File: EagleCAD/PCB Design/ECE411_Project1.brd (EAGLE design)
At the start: 160 x 100 mm, 24 parts

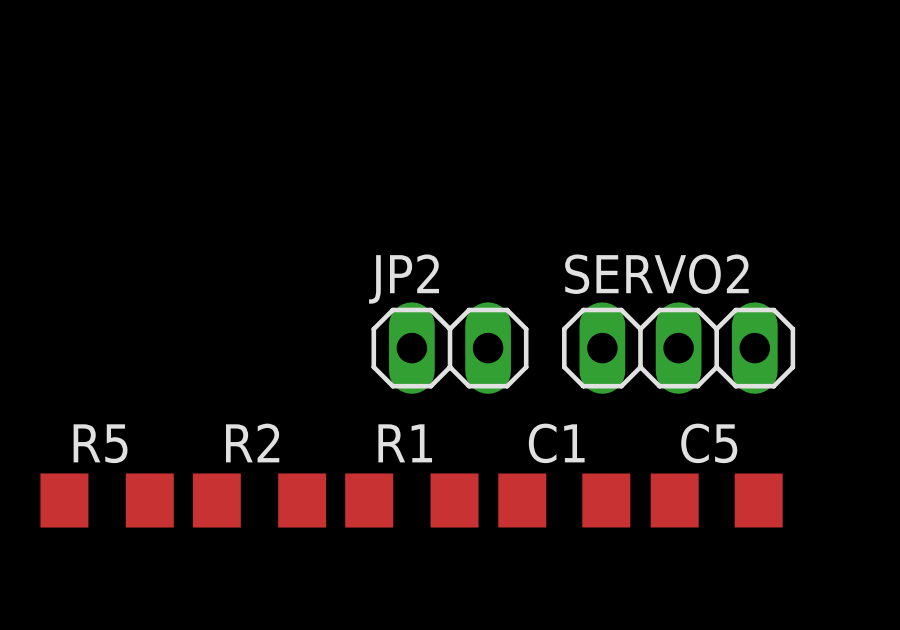
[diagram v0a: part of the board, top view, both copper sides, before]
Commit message: Added some custom library components, updated schematic with new xtal cap values, and updated links document
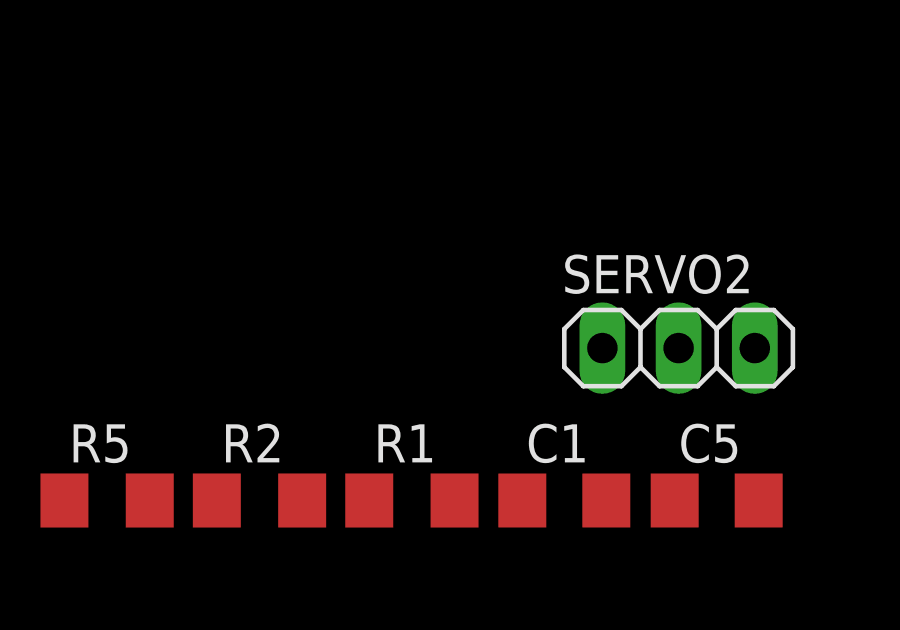
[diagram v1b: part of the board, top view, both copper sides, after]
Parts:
- removed JP2: (no value), pinhead:1X02
- C6, C7: value 12p -> 22p
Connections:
- net PWM1: now also SERVO1.1; no longer JP2.1
- net PWM2: now also SERVO2.1; no longer JP2.2
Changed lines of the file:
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@@
 <element name="CN1" library="adafruit" library_urn="urn:adsk.eagle:library:420" package="DCJACK_2MM_SMT" package3d_urn="urn:adsk.eagle:package:6240730/1" value="" x="-36.83" y="53.34"/>
 <element name="JP1" library="pinhead" library_urn="urn:adsk.eagle:library:325" package="2X03" package3d_urn="urn:adsk.eagle:package:22462/2" value="" x="-46.99" y="48.26"/>
-<element name="JP2" library="pinhead" library_urn="urn:adsk.eagle:library:325" package="1X02" package3d_urn="urn:adsk.eagle:package:22435/2" value="" x="-25.4" y="73.66"/>
 <element name="MICRO_USB_TYPE_B" library="adafruit" package="MOLEX_480371000" value="USB-A" x="-27.94" y="41.91">
 <attribute name="SPICEPREFIX" value="X" x="-27.94" y="41.91" size="1.778" layer="27" display="off"/>
@@
 <element name="LED2" library="led" library_urn="urn:adsk.eagle:library:259" package="1206" package3d_urn="urn:adsk.eagle:package:15796/1" value="" x="-67.31" y="-15.24"/>
 <element name="LED1" library="led" library_urn="urn:adsk.eagle:library:259" package="1206" package3d_urn="urn:adsk.eagle:package:15796/1" value="" x="-67.31" y="-20.32"/>
-<element name="C6" library="rcl" library_urn="urn:adsk.eagle:library:334" package="C1206" package3d_urn="urn:adsk.eagle:package:23618/2" value="12p" x="-67.31" y="-35.56">
+<element name="C6" library="rcl" library_urn="urn:adsk.eagle:library:334" package="C1206" package3d_urn="urn:adsk.eagle:package:23618/2" value="22p" x="-67.31" y="-35.56">
 <attribute name="SPICEPREFIX" value="C" x="-67.31" y="-35.56" size="1.778" layer="27" display="off"/>
 </element>
-<element name="C7" library="rcl" library_urn="urn:adsk.eagle:library:334" package="C1206" package3d_urn="urn:adsk.eagle:package:23618/2" value="12p" x="-67.31" y="-41.91">
+<element name="C7" library="rcl" library_urn="urn:adsk.eagle:library:334" package="C1206" package3d_urn="urn:adsk.eagle:package:23618/2" value="22p" x="-67.31" y="-41.91">
 <attribute name="SPICEPREFIX" value="C" x="-67.31" y="-41.91" size="1.778" layer="27" display="off"/>
 </element>
@@
 <signal name="PWM2">
 <contactref element="U$1" pad="29"/>
-<contactref element="JP2" pad="2"/>
-<wire x1="-47.54" y1="35.09" x2="-24.13" y2="73.66" width="0" layer="19" extent="1-1"/>
+<contactref element="SERVO2" pad="1"/>
+<wire x1="-47.54" y1="35.09" x2="-20.32" y2="73.66" width="0" layer="19" extent="1-1"/>
 </signal>
 <signal name="PWM1">
 <contactref element="U$1" pad="30"/>
-<contactref element="JP2" pad="1"/>
-<wire x1="-47.54" y1="35.89" x2="-26.67" y2="73.66" width="0" layer="19" extent="1-1"/>
+<contactref element="SERVO1" pad="1"/>
+<wire x1="-67.31" y1="66.04" x2="-47.54" y2="35.89" width="0" layer="19" extent="1-1"/>
 </signal>
 <signal name="N$15">

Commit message: Updated Schematic
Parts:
- removed 16MHZ: XTAL_ATS160SM-1, XTAL_ATS160SM-1:ATS160SM-1
- removed JP1: (no value), pinhead:2X03
- removed MICRO_USB_TYPE_B: USB-A, adafruit:MOLEX_480371000
- removed S1: SPST, adafruit:JUDCOSPST
- added ISP1: AVRISP-6, USB_Micro_and_AVRISP:AVRISP
- added J1: 0473460001_USBMICRO, USB_Micro_and_AVRISP:MOLEX_USBMICRO
- added SW1: FSM2JSMLTR, Push_Button:FSM2JSMLTR
- added U1: ATS160SM-1, Xtals:ATS160SM-1
- added U2: MIC29310-5.0WU, Regulators:TO-263/D2PAK
- added U3: NCP5501DT50RKG, Regulators:TO-263/D2PAK
- moved CN1 135.6 mm to (-87.6, -72.4)
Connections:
- removed net DC_PWR_5V_2A: CN1.PWR1
- removed net GNDBREAK: CN1.GND
- removed net N$14: SERVO1.2
- removed net N$19: SERVO2.2
- new net N$22: CN1.PWR1, U2.1, U3.1
- new net SERVO_PWR: SERVO1.2, SERVO2.2, U2.3
- net /RST: now also ISP1.5, SW1.1, SW1.3; no longer JP1.5, S1.T
- net GND: now also CN1.GND, ISP1.6, J1.5, J1.G1, J1.G2, J1.G3, J1.G4, J1.G5, J1.G6, SW1.2, SW1.4, U2.2, U3.2; no longer JP1.6, MICRO_USB_TYPE_B.4, S1.P
- net N$1: now also J1.3; no longer MICRO_USB_TYPE_B.3
- net N$15: now also ISP1.2; no longer JP1.2
- net N$16: now also ISP1.1; no longer JP1.1
- net N$17: now also ISP1.4; no longer JP1.4
- net N$18: now also ISP1.3; no longer JP1.3
- net N$20: now also U1.1; no longer 16MHZ.2
- net N$21: now also U1.2; no longer 16MHZ.1
- net N$3: now also J1.2; no longer MICRO_USB_TYPE_B.2
- net VBUS: now also J1.1; no longer MICRO_USB_TYPE_B.1
- net VCC: now also U3.3

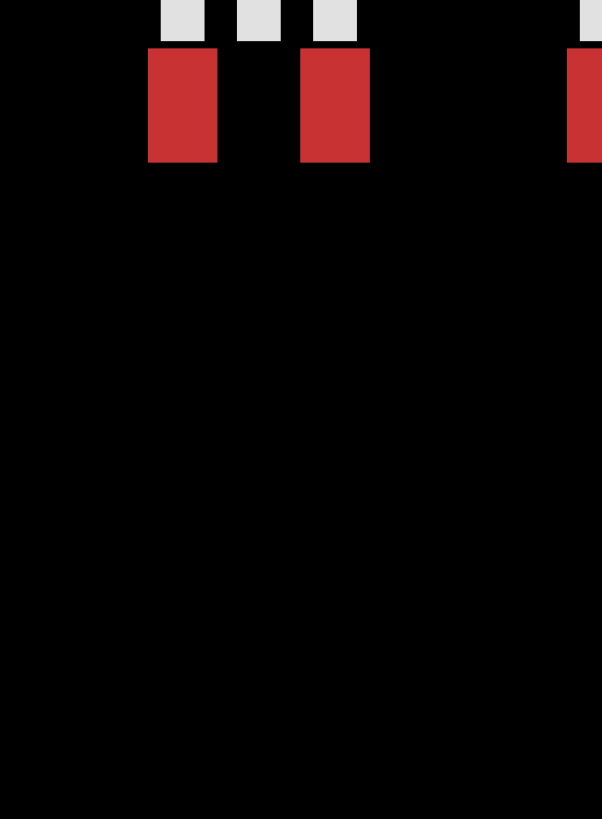
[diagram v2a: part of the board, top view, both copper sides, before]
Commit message: Visually complete schematic - nets need to be named still, and erc needs to be run.
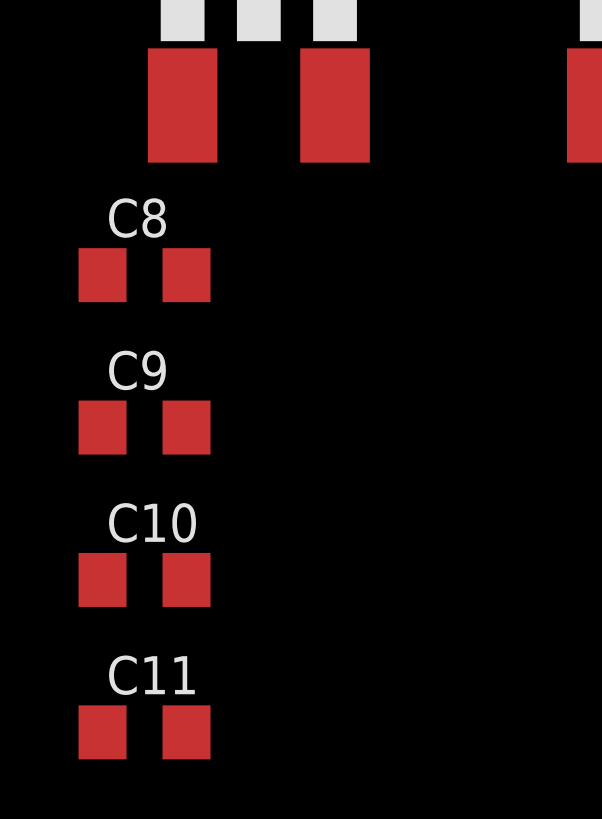
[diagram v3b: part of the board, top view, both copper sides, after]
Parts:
- added C10: 4.7u, rcl:C1206
- added C11, C9: 10u, rcl:C1206
- added C8: 0.1u, rcl:C1206
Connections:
- net GND: now also C10.2, C11.2, C8.2, C9.2
- net N$22: now also C8.1, C9.1
- net SERVO_PWR: now also C11.1
- net VCC: now also C10.1
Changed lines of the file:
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@@
 <element name="U2" library="Regulators" package="TO-263/D2PAK" value="MIC29310-5.0WU" x="-100.33" y="-69.85"/>
 <element name="U3" library="Regulators" package="TO-263/D2PAK" value="NCP5501DT50RKG" x="-114.3" y="-69.85"/>
+<element name="C8" library="rcl" library_urn="urn:adsk.eagle:library:334" package="C1206" package3d_urn="urn:adsk.eagle:package:23618/2" value="0.1u" x="-118.11" y="-82.55">
+<attribute name="SPICEPREFIX" value="C" x="-118.11" y="-82.55" size="1.778" layer="27" display="off"/>
+</element>
+<element name="C9" library="rcl" library_urn="urn:adsk.eagle:library:334" package="C1206" package3d_urn="urn:adsk.eagle:package:23618/2" value="10u" x="-118.11" y="-87.63">
+<attribute name="SPICEPREFIX" value="C" x="-118.11" y="-87.63" size="1.778" layer="27" display="off"/>
+</element>
+<element name="C10" library="rcl" library_urn="urn:adsk.eagle:library:334" package="C1206" package3d_urn="urn:adsk.eagle:package:23618/2" value="4.7u" x="-118.11" y="-92.71">
+<attribute name="SPICEPREFIX" value="C" x="-118.11" y="-92.71" size="1.778" layer="27" display="off"/>
+</element>
+<element name="C11" library="rcl" library_urn="urn:adsk.eagle:library:334" package="C1206" package3d_urn="urn:adsk.eagle:package:23618/2" value="10u" x="-118.11" y="-97.79">
+<attribute name="SPICEPREFIX" value="C" x="-118.11" y="-97.79" size="1.778" layer="27" display="off"/>
+</element>
 </elements>
 <signals>
@@
 <contactref element="CN1" pad="GND"/>
 <contactref element="CN1" pad="GNDBREAK"/>
+<contactref element="C8" pad="2"/>
+<contactref element="C11" pad="2"/>
+<contactref element="C9" pad="2"/>
+<contactref element="C10" pad="2"/>
+<wire x1="-116.71" y1="-92.71" x2="-116.71" y2="-97.79" width="0" layer="19" extent="1-1"/>
+<wire x1="-116.71" y1="-87.63" x2="-116.71" y2="-92.71" width="0" layer="19" extent="1-1"/>
+<wire x1="-116.71" y1="-82.55" x2="-116.71" y2="-87.63" width="0" layer="19" extent="1-1"/>
+<wire x1="-114.3" y1="-65.725" x2="-116.71" y2="-82.55" width="0" layer="19" extent="1-1"/>
 <wire x1="-100.33" y1="-65.725" x2="-114.3" y2="-65.725" width="0" layer="19" extent="1-1"/>
 <wire x1="-87.63" y1="-77.89" x2="-100.33" y2="-65.725" width="0" layer="19" extent="1-1"/>
@@
 <contactref element="C5" pad="2"/>
 <contactref element="U3" pad="3"/>
+<contactref element="C10" pad="1"/>
+<wire x1="-111.76" y1="-76.895" x2="-119.51" y2="-92.71" width="0" layer="19" extent="1-1"/>
 <wire x1="-55.74" y1="28.49" x2="-111.76" y2="-76.895" width="0" layer="19" extent="1-1"/>
 <wire x1="-47.54" y1="31.09" x2="-55.74" y2="28.49" width="0" layer="19" extent="1-1"/>
@@
 <contactref element="SERVO2" pad="2"/>
 <contactref element="U2" pad="3"/>
+<contactref element="C11" pad="1"/>
+<wire x1="-97.79" y1="-76.895" x2="-119.51" y2="-97.79" width="0" layer="19" extent="1-1"/>
 <wire x1="-64.77" y1="66.04" x2="-97.79" y2="-76.895" width="0" layer="19" extent="1-1"/>
 <wire x1="-17.78" y1="73.66" x2="-64.77" y2="66.04" width="0" layer="19" extent="1-1"/>
@@
 <contactref element="U3" pad="1"/>
 <contactref element="U2" pad="1"/>
+<contactref element="C8" pad="1"/>
+<contactref element="C9" pad="1"/>
+<wire x1="-119.51" y1="-82.55" x2="-119.51" y2="-87.63" width="0" layer="19" extent="1-1"/>
+<wire x1="-116.84" y1="-76.895" x2="-119.51" y2="-82.55" width="0" layer="19" extent="1-1"/>
 <wire x1="-102.87" y1="-76.895" x2="-116.84" y2="-76.895" width="0" layer="19" extent="1-1"/>
 <wire x1="-87.63" y1="-66.89" x2="-102.87" y2="-76.895" width="0" layer="19" extent="1-1"/>

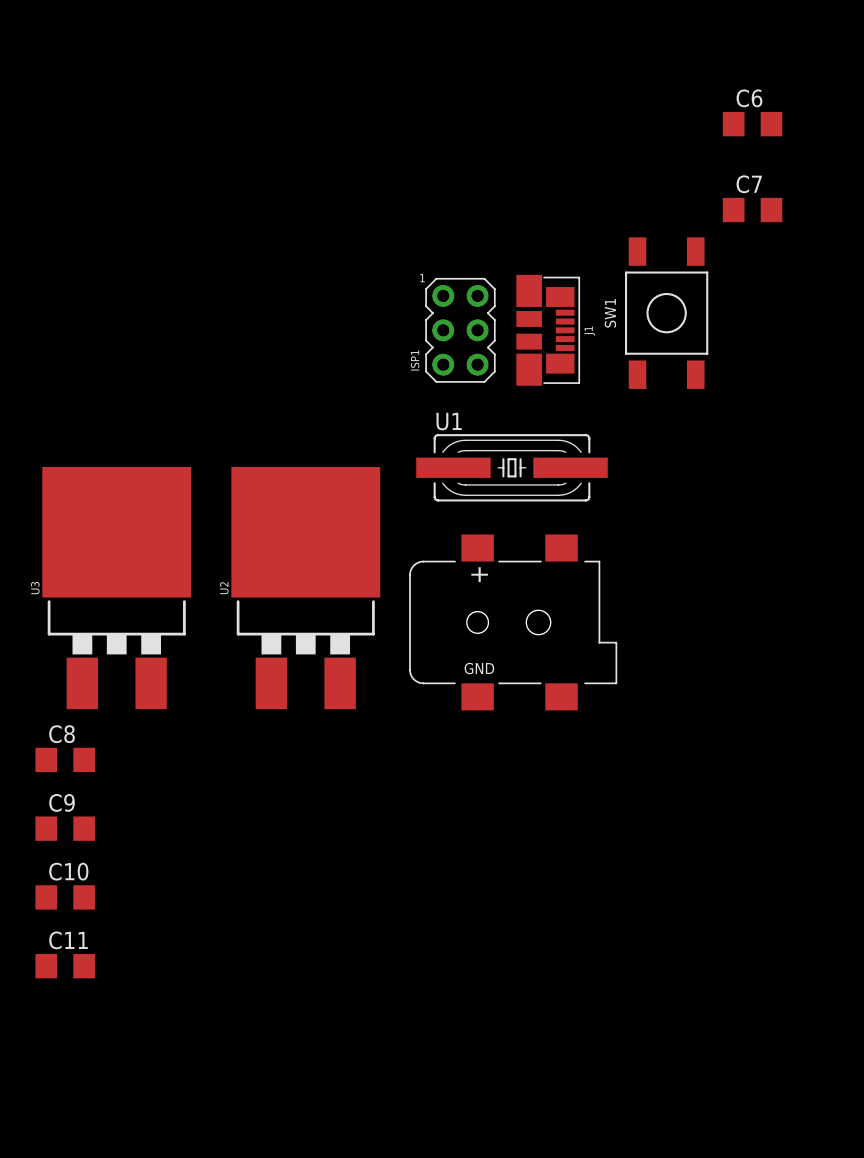
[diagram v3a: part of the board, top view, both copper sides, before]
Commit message: changed xtal caps to 0805 size from 1206
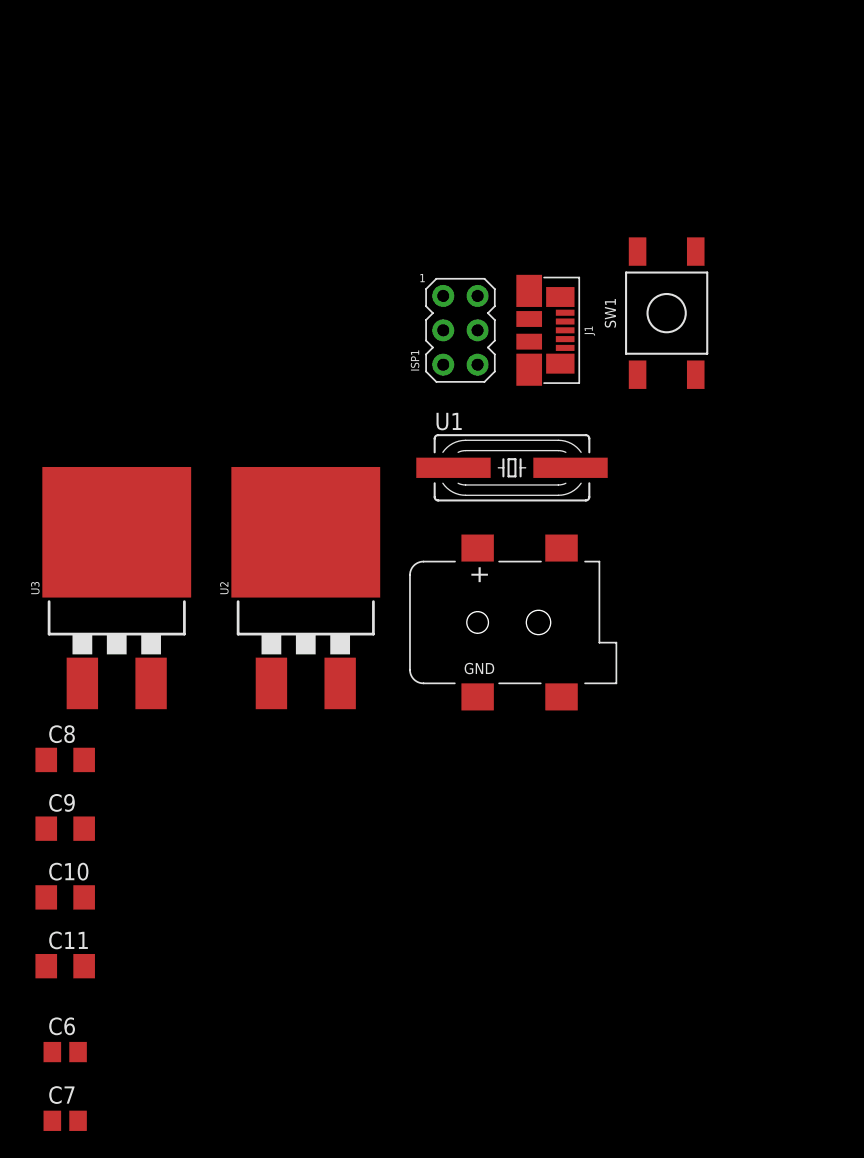
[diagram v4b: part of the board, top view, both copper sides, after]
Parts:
- C6, C7: device rcl:C1206 -> rcl:C0805
- moved C6 85.3 mm to (-118.1, -104.1)
- moved C7 84.3 mm to (-118.1, -109.2)
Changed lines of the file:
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@@
 <element name="LED2" library="led" library_urn="urn:adsk.eagle:library:259" package="1206" package3d_urn="urn:adsk.eagle:package:15796/1" value="" x="-67.31" y="-15.24"/>
 <element name="LED1" library="led" library_urn="urn:adsk.eagle:library:259" package="1206" package3d_urn="urn:adsk.eagle:package:15796/1" value="" x="-67.31" y="-20.32"/>
-<element name="C6" library="rcl" library_urn="urn:adsk.eagle:library:334" package="C1206" package3d_urn="urn:adsk.eagle:package:23618/2" value="22p" x="-67.31" y="-35.56">
-<attribute name="SPICEPREFIX" value="C" x="-67.31" y="-35.56" size="1.778" layer="27" display="off"/>
-</element>
-<element name="C7" library="rcl" library_urn="urn:adsk.eagle:library:334" package="C1206" package3d_urn="urn:adsk.eagle:package:23618/2" value="22p" x="-67.31" y="-41.91">
-<attribute name="SPICEPREFIX" value="C" x="-67.31" y="-41.91" size="1.778" layer="27" display="off"/>
-</element>
 <element name="SW1" library="Push_Button" package="FSM2JSMLTR" value="FSM2JSMLTR" x="-73.66" y="-49.53"/>
 <element name="J1" library="USB_Micro_and_AVRISP" package="MOLEX_USBMICRO" value="0473460001_USBMICRO" x="-83.82" y="-50.8"/>
@@
 <element name="C11" library="rcl" library_urn="urn:adsk.eagle:library:334" package="C1206" package3d_urn="urn:adsk.eagle:package:23618/2" value="10u" x="-118.11" y="-97.79">
 <attribute name="SPICEPREFIX" value="C" x="-118.11" y="-97.79" size="1.778" layer="27" display="off"/>
+</element>
+<element name="C6" library="rcl" library_urn="urn:adsk.eagle:library:334" package="C0805" package3d_urn="urn:adsk.eagle:package:23617/2" value="22p" x="-118.11" y="-104.14">
+<attribute name="SPICEPREFIX" value="C" x="-118.11" y="-104.14" size="1.778" layer="27" display="off"/>
+</element>
+<element name="C7" library="rcl" library_urn="urn:adsk.eagle:library:334" package="C0805" package3d_urn="urn:adsk.eagle:package:23617/2" value="22p" x="-118.11" y="-109.22">
+<attribute name="SPICEPREFIX" value="C" x="-118.11" y="-109.22" size="1.778" layer="27" display="off"/>
 </element>
 </elements>
@@
 <contactref element="BUTTON_PAD" pad="5"/>
 <contactref element="LED2" pad="C"/>
-<contactref element="C6" pad="1"/>
-<contactref element="C7" pad="1"/>
 <contactref element="C2" pad="1"/>
 <contactref element="C5" pad="1"/>
@@
 <contactref element="C9" pad="2"/>
 <contactref element="C10" pad="2"/>
+<contactref element="C6" pad="1"/>
+<contactref element="C7" pad="1"/>
+<wire x1="-119.06" y1="-104.14" x2="-119.06" y2="-109.22" width="0" layer="19" extent="1-1"/>
+<wire x1="-116.71" y1="-97.79" x2="-119.06" y2="-104.14" width="0" layer="19" extent="1-1"/>
 <wire x1="-116.71" y1="-92.71" x2="-116.71" y2="-97.79" width="0" layer="19" extent="1-1"/>
 <wire x1="-116.71" y1="-87.63" x2="-116.71" y2="-92.71" width="0" layer="19" extent="1-1"/>
@@
 <wire x1="-75.81" y1="-54.08" x2="-81.16" y2="-52.1" width="0" layer="19" extent="1-1"/>
 <wire x1="-71.51" y1="-54.08" x2="-75.81" y2="-54.08" width="0" layer="19" extent="1-1"/>
-<wire x1="-68.71" y1="-41.91" x2="-71.51" y2="-54.08" width="0" layer="19" extent="1-1"/>
-<wire x1="-68.71" y1="-35.56" x2="-68.71" y2="-41.91" width="0" layer="19" extent="1-1"/>
-<wire x1="-65.888" y1="-20.32" x2="-68.71" y2="-35.56" width="0" layer="19" extent="1-1"/>
+<wire x1="-65.888" y1="-20.32" x2="-81.52" y2="-48.3375" width="0" layer="19" extent="1-1"/>
 <wire x1="-65.888" y1="-15.24" x2="-65.888" y2="-20.32" width="0" layer="19" extent="1-1"/>
 <wire x1="-54.94" y1="28.49" x2="-65.888" y2="-15.24" width="0" layer="19" extent="1-1"/>
@@
 </signal>
 <signal name="N$20">
-<contactref element="C7" pad="2"/>
 <contactref element="U$1" pad="16"/>
 <contactref element="U1" pad="1"/>
-<wire x1="-65.91" y1="-41.91" x2="-89.416" y2="-60.96" width="0" layer="19" extent="1-1"/>
-<wire x1="-54.14" y1="28.49" x2="-65.91" y2="-41.91" width="0" layer="19" extent="1-1"/>
+<contactref element="C7" pad="2"/>
+<wire x1="-89.416" y1="-60.96" x2="-117.16" y2="-109.22" width="0" layer="19" extent="1-1"/>
+<wire x1="-54.14" y1="28.49" x2="-89.416" y2="-60.96" width="0" layer="19" extent="1-1"/>
 </signal>
 <signal name="N$21">
-<contactref element="C6" pad="2"/>
 <contactref element="U$1" pad="17"/>
 <contactref element="U1" pad="2"/>
-<wire x1="-65.91" y1="-35.56" x2="-80.764" y2="-60.96" width="0" layer="19" extent="1-1"/>
-<wire x1="-53.34" y1="28.49" x2="-65.91" y2="-35.56" width="0" layer="19" extent="1-1"/>
+<contactref element="C6" pad="2"/>
+<wire x1="-80.764" y1="-60.96" x2="-117.16" y2="-104.14" width="0" layer="19" extent="1-1"/>
+<wire x1="-53.34" y1="28.49" x2="-80.764" y2="-60.96" width="0" layer="19" extent="1-1"/>
 </signal>
 <signal name="VBUS">
